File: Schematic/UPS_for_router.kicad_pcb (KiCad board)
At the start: 2 copper layers, 90 x 70 mm, 23 parts, among them J1 12V-IN, J2 12V-IN, J3 BAT IN, J4 12V-OUT, J5 9V-OUT, J6 12V out, K1 FINDER-36.11, SW1 SW_SPST, U1 L7809

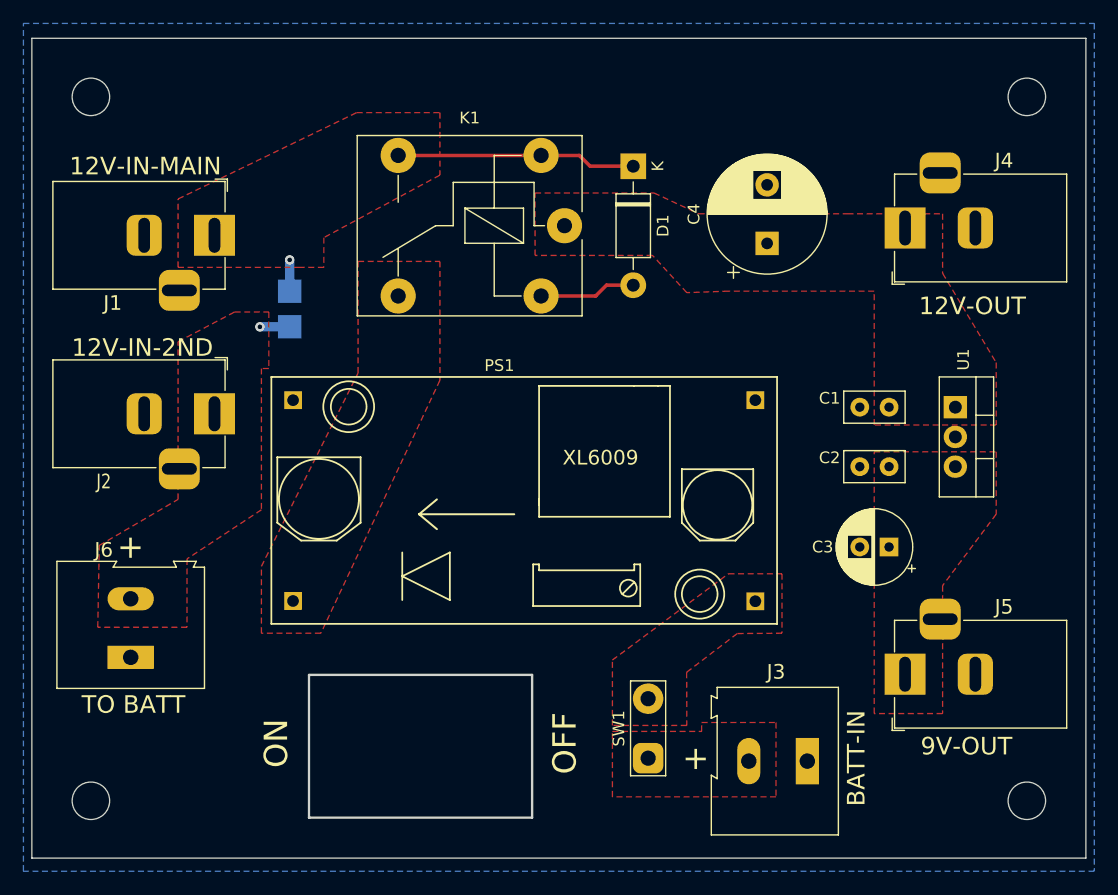
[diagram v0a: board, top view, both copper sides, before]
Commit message: updated schematic and PCB
removed relay and added diode as well as updated the PCB
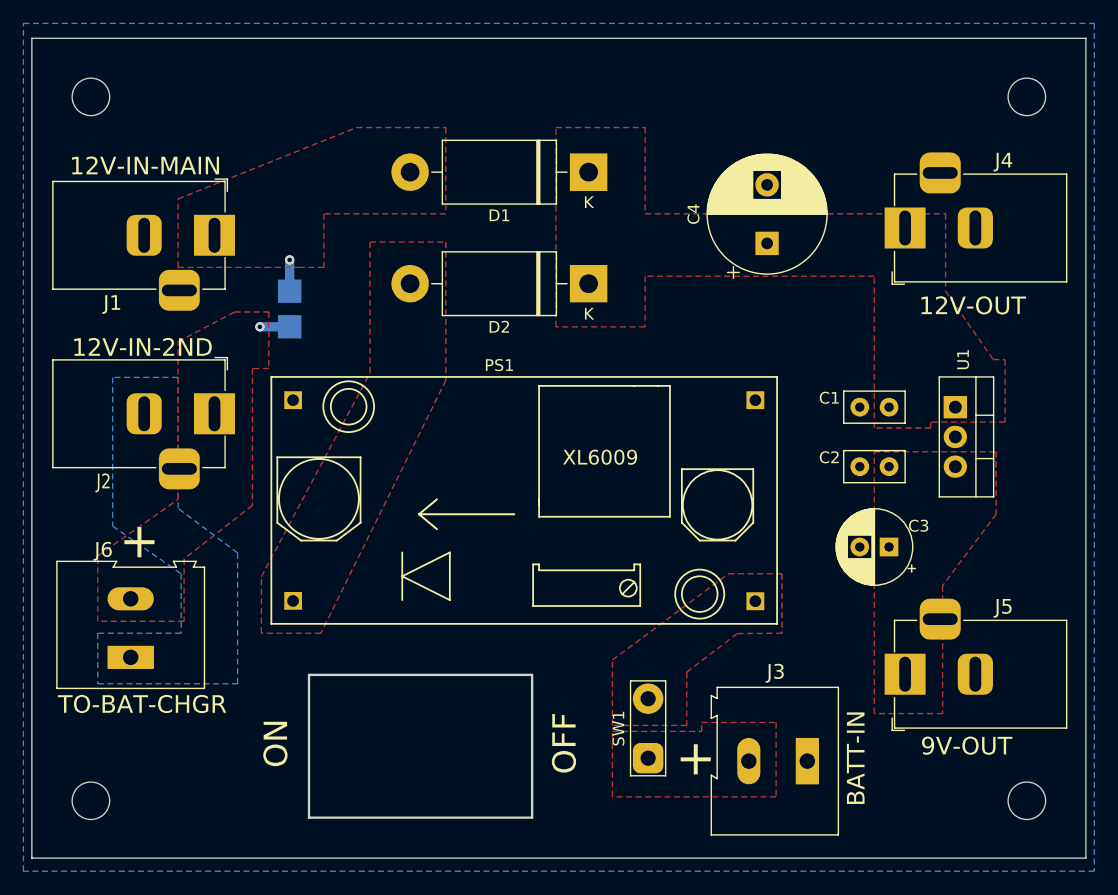
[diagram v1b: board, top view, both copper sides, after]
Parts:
- removed K1: FINDER-36.11, Relay_THT:Relay_SPDT_Finder_36.11
- added D2: 1N5822, Diode_THT:D_DO-201AD_P15.24mm_Horizontal, F.Cu at (141.0, 79.4)
- D1: value 1N4007 -> 1N5822; footprint Diode_THT:D_DO-41_SOD81_P10.16mm_Horizontal -> Diode_THT:D_DO-201AD_P15.24mm_Horizontal
- moved D1 3.84 mm to (141.0, 69.8), turned to 180 degrees
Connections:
- D1 pad 1: /12V-main -> /12V-OUT
- D1 pad 2: GND -> /12V-main
- J2 pad 2: GND -> GND1
- J6 pad 1: GND -> GND1
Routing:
- net /12V-main: track 23.0 -> 2.67 mm
- net GND: track 8.17 -> 0.00 mm
- added copper zone on B.Cu, net GND1
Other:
- board text added: "TO-BAT-CHGR"
- board text removed: "TO BATT"
